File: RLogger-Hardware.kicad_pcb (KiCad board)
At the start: 2 copper layers, 13 parts, among them J1 Bat Connector, J2 Baro, J3 FRAM, J4 MicroSD, J5 BMI160, U1 MIC2288BD5

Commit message: PCB done :o
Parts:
- moved J1 31.9 mm to (152.5, 106.5), turned to 180 degrees
- moved J4 14.9 mm to (132.0, 50.5)
- moved J2 14.6 mm to (143.0, 75.5)
- moved C1 14.5 mm to (149.5, 59.5)
- moved C2 14.5 mm to (133.0, 60.0)
- moved D1 14.5 mm to (138.0, 62.5)
- moved L1 14.5 mm to (144.5, 62.5)
- moved R1 14.5 mm to (137.0, 57.5)
- moved R2 14.5 mm to (140.5, 58.0)
- moved U1 14.5 mm to (144.7, 59.3)
- moved J3 14.5 mm to (130.5, 70.4)
- moved J5 14.5 mm to (128.5, 75.5)
- moved A1 12.4 mm to (132.0, 98.5)
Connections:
- A1 pad 12: /CS -> /SS1
- A1 pad 13: /CS -> /SS0
- A1 pad 27: /+5V5 -> /+5V
- C2 pad 1: /+5V5 -> /+5V
- D1 pad 1: /+5V5 -> /+5V
- J2 pad 1: /+5V5 -> /+5V
- J2 pad 7: /+5V5 -> /+5V
- J3 pad 7: /CS -> /SS0
- J4 pad 7: /CS -> /SS1
- R1 pad 1: /+5V5 -> /+5V
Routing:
- net /SS1: track 0.00 -> 103.3 mm, vias 0 -> 2
- net /SCK: track 0.00 -> 98.6 mm
- net /DO: track 0.00 -> 92.2 mm
- net /+5V: track 0.00 -> 86.9 mm, vias 0 -> 1
- net /DI: track 0.00 -> 86.3 mm
- net /SS0: track 0.00 -> 66.1 mm, vias 0 -> 2
- net /SCL: track 0.00 -> 53.8 mm
- net +BATT: track 0.00 -> 53.0 mm, vias 0 -> 2
- net /SDA: track 0.00 -> 50.5 mm
- net GND: track 0.00 -> 22.0 mm, vias 0 -> 10
- net Net-(R1-Pad2): track 0.00 -> 6.11 mm
- net Net-(D1-Pad2): track 0.00 -> 6.00 mm
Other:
- board outline added: 29 x 114 mm
- board text added: "+"
- board text added: "-"
- board text added: "RLogger V1"
- board text added: "by nachocpol"

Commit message: Working on the PCB layout
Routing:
- net GND: track 22.0 -> 24.5 mm, vias 10 -> 12
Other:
- rule via_min_size: 0.4 -> 0.3
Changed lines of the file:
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@@
     (thickness 1.6)
     (drawings 30)
-    (tracks 120)
+    (tracks 123)
     (zones 0)
     (modules 13)
@@
   (page A4)
   (layers
-    (0 F.Cu signal)
-    (31 B.Cu signal)
+    (0 F.Cu signal hide)
+    (31 B.Cu signal hide)
     (32 B.Adhes user)
     (33 F.Adhes user)
@@
     (via_size 0.8)
     (via_drill 0.4)
-    (via_min_size 0.4)
+    (via_min_size 0.3)
     (via_min_drill 0.3)
     (uvia_size 0.3)
@@
       (psa4output false)
       (plotreference true)
-      (plotvalue true)
+      (plotvalue false)
       (plotinvisibletext false)
       (padsonsilk false)
@@
       (outputformat 1)
       (mirror false)
-      (drillshape 1)
+      (drillshape 0)
       (scaleselection 1)
-      (outputdirectory ""))
+      (outputdirectory "Fabrication/"))
   )
   (net 0 "")
@@
       (effects (font (size 0.5 0.5) (thickness 0.08)) (justify mirror))
     )
-    (pad 1 smd roundrect (at -1.025 0 270) (size 1.15 1.4) (layers B.Cu B.Paste B.Mask) (roundrect_rratio 0.217391)
+    (pad 1 smd roundrect (at -1.025 0 270) (size 1.15 1.4) (layers B.Cu B.Paste B.Mask) (roundrect_rratio 0.2173904347826087)
       (net 27 +BATT))
-    (pad 2 smd roundrect (at 1.025 0 270) (size 1.15 1.4) (layers B.Cu B.Paste B.Mask) (roundrect_rratio 0.217391)
+    (pad 2 smd roundrect (at 1.025 0 270) (size 1.15 1.4) (layers B.Cu B.Paste B.Mask) (roundrect_rratio 0.2173904347826087)
       (net 7 GND))
     (model ${KISYS3DMOD}/Capacitor_SMD.3dshapes/C_0805_2012Metric.wrl
@@
     (fp_line (start -1.6 0.8) (end 1.6 0.8) (layer B.Fab) (width 0.1))
     (fp_line (start -1.6 -0.8) (end -1.6 0.8) (layer B.Fab) (width 0.1))
-    (fp_text user %R (at 0 0 90) (layer B.Fab)
+    (fp_text user %R (at 0 0 90) (layer B.Fab) hide
       (effects (font (size 0.8 0.8) (thickness 0.12)) (justify mirror))
     )
-    (pad 1 smd roundrect (at -1.5625 0 270) (size 1.325 1.8) (layers B.Cu B.Paste B.Mask) (roundrect_rratio 0.188679)
+    (pad 1 smd roundrect (at -1.5625 0 270) (size 1.325 1.8) (layers B.Cu B.Paste B.Mask) (roundrect_rratio 0.1886784905660377)
       (net 31 /+5V))
-    (pad 2 smd roundrect (at 1.5625 0 270) (size 1.325 1.8) (layers B.Cu B.Paste B.Mask) (roundrect_rratio 0.188679)
+    (pad 2 smd roundrect (at 1.5625 0 270) (size 1.325 1.8) (layers B.Cu B.Paste B.Mask) (roundrect_rratio 0.1886784905660377)
       (net 7 GND))
     (model ${KISYS3DMOD}/Capacitor_SMD.3dshapes/C_1206_3216Metric.wrl
@@
     (tags Powermite)
     (attr smd)
-    (fp_text reference D1 (at -1 2.5) (layer B.SilkS)
+    (fp_text reference D1 (at -1 2.5) (layer B.SilkS) hide
       (effects (font (size 1 1) (thickness 0.15)) (justify mirror))
     )
@@
     (tags "inductor handsolder")
     (attr smd)
-    (fp_text reference L1 (at 0 -1.5) (layer B.SilkS)
+    (fp_text reference L1 (at 0 -2) (layer B.SilkS) hide
       (effects (font (size 1 1) (thickness 0.15)) (justify mirror))
     )
@@
       (effects (font (size 0.5 0.5) (thickness 0.08)) (justify mirror))
     )
-    (pad 1 smd roundrect (at -1.15 0 180) (size 1.05 1.2) (layers B.Cu B.Paste B.Mask) (roundrect_rratio 0.238095)
+    (pad 1 smd roundrect (at -1.15 0 180) (size 1.05 1.2) (layers B.Cu B.Paste B.Mask) (roundrect_rratio 0.2380942857142857)
       (net 27 +BATT))
-    (pad 2 smd roundrect (at 1.15 0 180) (size 1.05 1.2) (layers B.Cu B.Paste B.Mask) (roundrect_rratio 0.238095)
+    (pad 2 smd roundrect (at 1.15 0 180) (size 1.05 1.2) (layers B.Cu B.Paste B.Mask) (roundrect_rratio 0.2380942857142857)
       (net 28 "Net-(D1-Pad2)"))
     (model ${KISYS3DMOD}/Inductor_SMD.3dshapes/L_0805_2012Metric.wrl
@@
       (effects (font (size 0.5 0.5) (thickness 0.08)) (justify mirror))
     )
-    (pad 2 smd roundrect (at 1.025 0) (size 1.15 1.4) (layers B.Cu B.Paste B.Mask) (roundrect_rratio 0.217391)
+    (pad 2 smd roundrect (at 1.025 0) (size 1.15 1.4) (layers B.Cu B.Paste B.Mask) (roundrect_rratio 0.2173904347826087)
       (net 40 "Net-(R1-Pad2)"))
-    (pad 1 smd roundrect (at -1.025 0) (size 1.15 1.4) (layers B.Cu B.Paste B.Mask) (roundrect_rratio 0.217391)
+    (pad 1 smd roundrect (at -1.025 0) (size 1.15 1.4) (layers B.Cu B.Paste B.Mask) (roundrect_rratio 0.2173904347826087)
       (net 31 /+5V))
     (model ${KISYS3DMOD}/Resistor_SMD.3dshapes/R_0805_2012Metric.wrl
@@
       (effects (font (size 0.5 0.5) (thickness 0.08)) (justify mirror))
     )
-    (pad 1 smd roundrect (at -1.025 0 270) (size 1.15 1.4) (layers B.Cu B.Paste B.Mask) (roundrect_rratio 0.217391)
+    (pad 1 smd roundrect (at -1.025 0 270) (size 1.15 1.4) (layers B.Cu B.Paste B.Mask) (roundrect_rratio 0.2173904347826087)
       (net 40 "Net-(R1-Pad2)"))
-    (pad 2 smd roundrect (at 1.025 0 270) (size 1.15 1.4) (layers B.Cu B.Paste B.Mask) (roundrect_rratio 0.217391)
+    (pad 2 smd roundrect (at 1.025 0 270) (size 1.15 1.4) (layers B.Cu B.Paste B.Mask) (roundrect_rratio 0.2173904347826087)
       (net 7 GND))
     (model ${KISYS3DMOD}/Resistor_SMD.3dshapes/R_0805_2012Metric.wrl
@@
   (segment (start 145.25 97.5) (end 147 95.75) (width 0.25) (layer F.Cu) (net 7))
   (segment (start 144.5 97.5) (end 145.25 97.5) (width 0.25) (layer F.Cu) (net 7))
+  (via (at 141.5 61.25) (size 0.8) (drill 0.4) (layers F.Cu B.Cu) (net 7))
+  (via (at 141.5 63.75) (size 0.8) (drill 0.4) (layers F.Cu B.Cu) (net 7))
+  (segment (start 141.5 61.25) (end 141.5 63.75) (width 0.25) (layer F.Cu) (net 7))
   (via (at 143.25 106.25) (size 0.8) (drill 0.4) (layers F.Cu B.Cu) (net 31))
   (via (at 153 81.5) (size 0.8) (drill 0.4) (layers F.Cu B.Cu) (net 27))

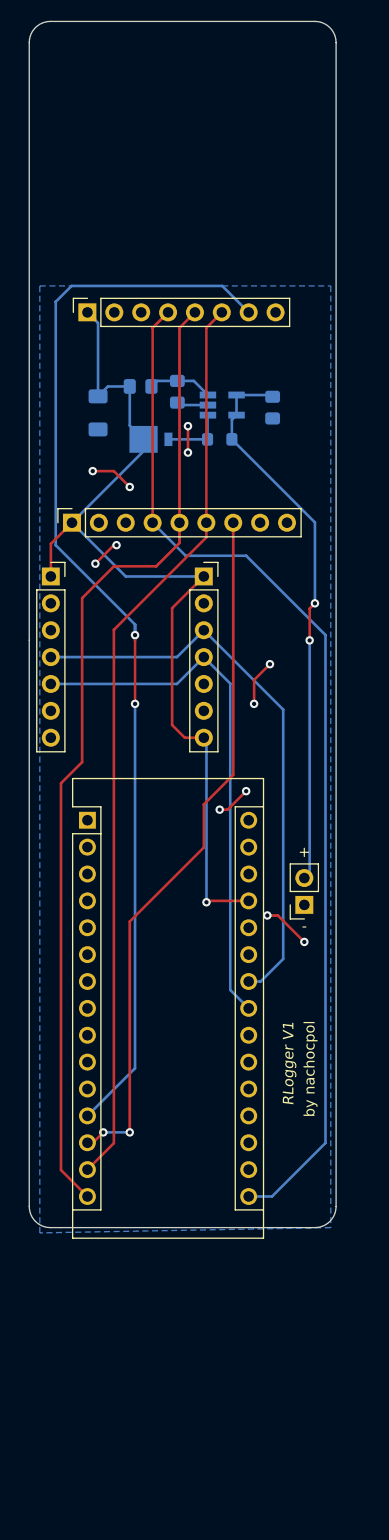
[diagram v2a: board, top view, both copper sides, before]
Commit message: Added mounting holes. Updated PCB layout. Generated fabrication files.
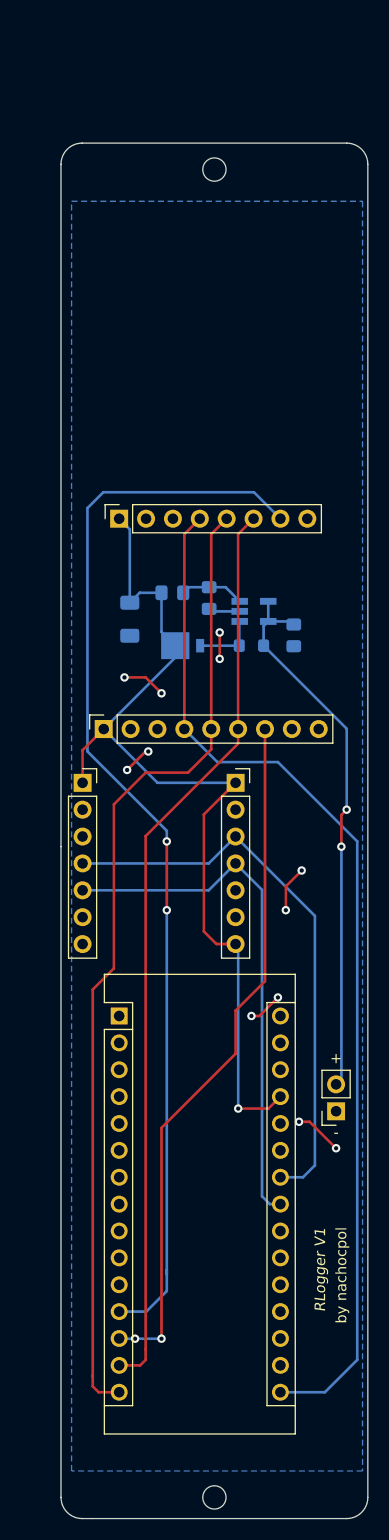
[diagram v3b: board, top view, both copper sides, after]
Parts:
- added H1: MountingHole, MountingHole:MountingHole_2.2mm_M2, F.Cu at (144.0, 37.0)
- added H2: MountingHole, MountingHole:MountingHole_2.2mm_M2, F.Cu at (144.0, 162.5)
- moved C1 21.6 mm to (151.5, 81.0)
- moved U1 19.7 mm to (147.7, 78.8)
- moved C2 19.7 mm to (136.0, 79.5)
- moved D1 19.7 mm to (141.0, 82.0)
- moved J1 19.7 mm to (155.5, 126.0)
- moved J2 19.7 mm to (146.0, 95.0)
- moved J3 19.7 mm to (133.5, 89.9)
- moved J4 19.7 mm to (135.0, 70.0)
- moved J5 19.7 mm to (131.5, 95.0)
- moved L1 19.7 mm to (147.5, 82.0)
- moved R1 19.7 mm to (140.0, 77.0)
- moved R2 19.7 mm to (143.5, 77.5)
- moved A1 18.7 mm to (135.0, 117.0)
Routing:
- net +BATT: track 53.0 -> 52.0 mm
- net /+5V: track 86.9 -> 87.5 mm
- net /SS1: track 103.3 -> 102.7 mm
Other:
- board size 29 x 114 mm -> 29 x 130 mm
